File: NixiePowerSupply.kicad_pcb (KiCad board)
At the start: 2 copper layers, 41.5 x 41.5 mm, 20 parts, among them J1 Conn_01x02, J2 Conn_01x02, Q1 IRF740, Q2 2N3905, U1 MC34063AP

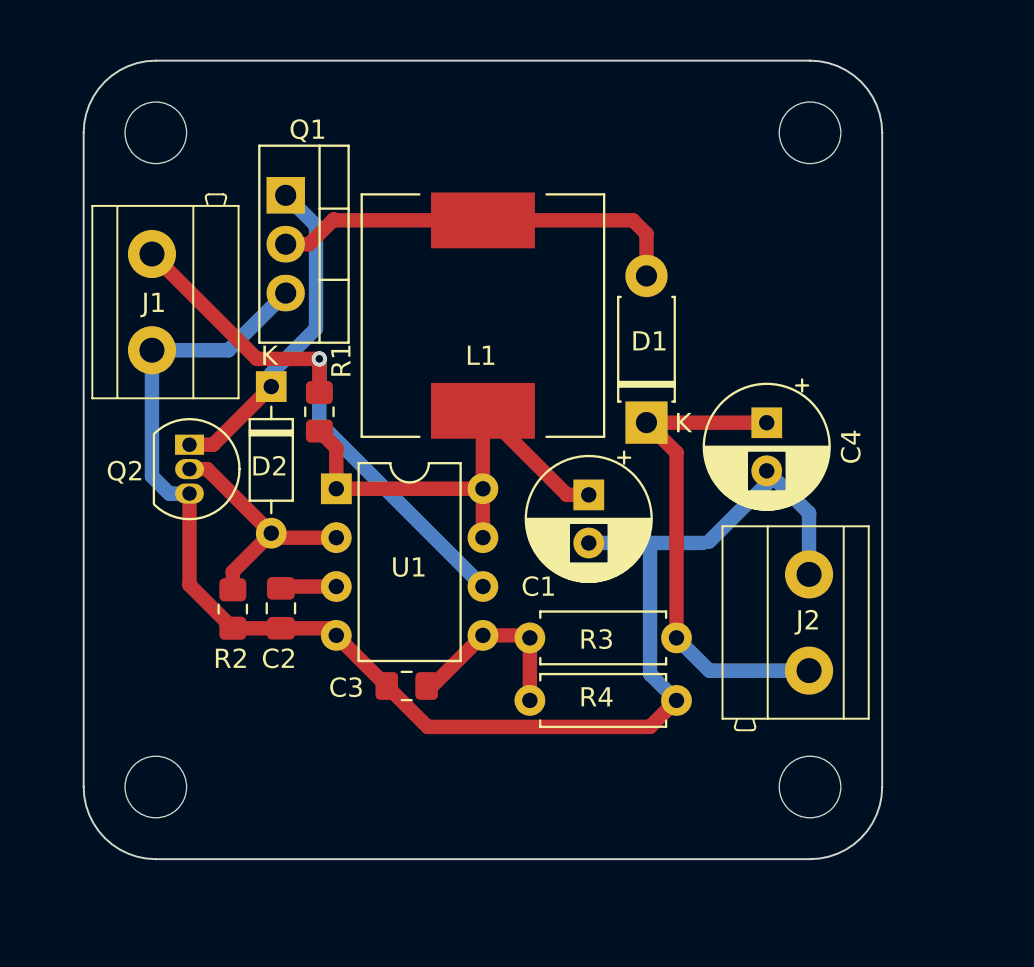
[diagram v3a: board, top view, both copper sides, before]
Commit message: add filling gnd
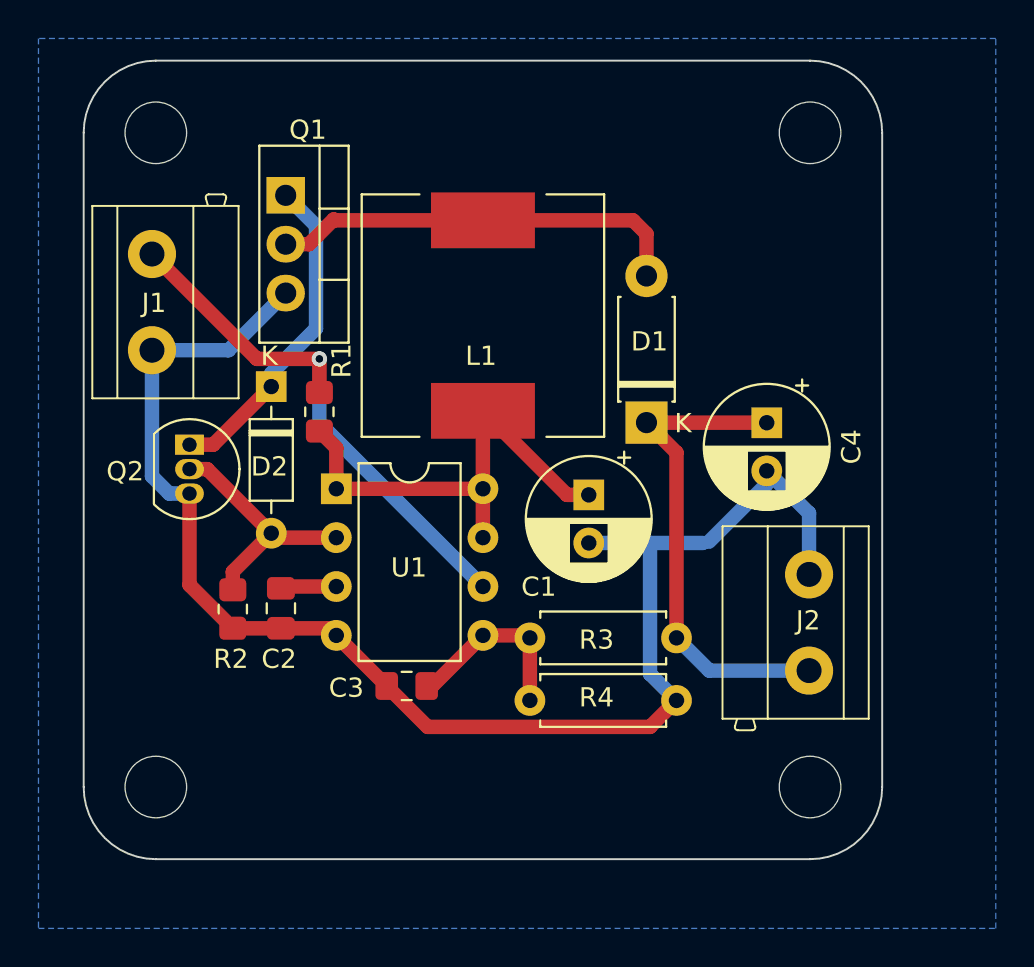
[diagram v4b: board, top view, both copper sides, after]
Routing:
- added copper zone on B.Cu, net GND
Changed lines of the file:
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@@
   (segment (start 101.84835 131.48165) (end 101.84835 128.15165) (width 0.75) (layer "B.Cu") (net 9))
   (segment (start 110.34835 139.98165) (end 101.84835 131.48165) (width 0.75) (layer "B.Cu") (net 9))
+  (zone (net 2) (net_name "GND") (layer "B.Cu") (name "gnd") (hatch edge 0.5)
+    (connect_pads (clearance 0.5))
+    (min_thickness 0.25) (filled_areas_thickness no)
+    (fill yes (thermal_gap 0.5) (thermal_bridge_width 0.5))
+    (polygon
+      (pts
+        (xy 137 157.75)
+        (xy 137 111.5)
+        (xy 87.25 111.5)
+        (xy 87.25 157.75)
+      )
+    )
+  )
 )
